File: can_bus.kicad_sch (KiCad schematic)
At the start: 1 part, among them U8 MCP2562-E-SN

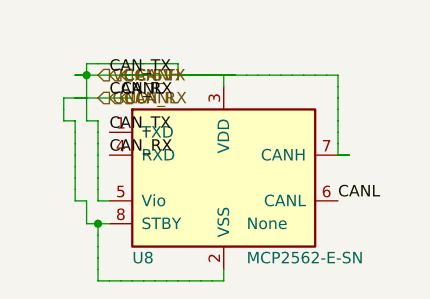
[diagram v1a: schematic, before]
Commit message: fix router map cell no more mark for pins
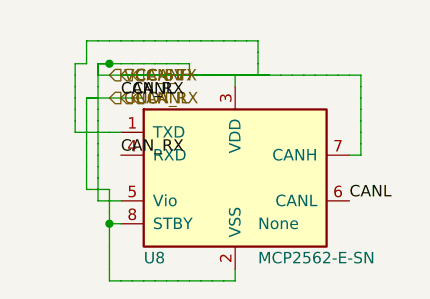
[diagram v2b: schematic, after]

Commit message: fix writer
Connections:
- net CANH: no longer U8.2 (VSS), U8.4 (RXD), U8.6 (CANL), U8.8 (STBY)
- new net CANL: U8.2 (VSS), U8.4 (RXD), U8.6 (CANL), U8.8 (STBY)

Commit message: реализована 2я занятость клетки
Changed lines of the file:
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@@
 		(instances
 			(project "Untitled"
-				(path "/1b7fa113-8fb8-4ba3-aa4e-c282a201fa61"
+				(path "/0ab84049-60df-40f5-bc1e-adacfd33f524"
 					(reference "U8")
 					(unit 1)
@@
 	(wire
 		(pts
-			(xy 21.59 29.21) (xy 21.59 25.4)
+			(xy 21.59 29.21) (xy 19.05 29.21)
 		)
 		(stroke
@@
 	(wire
 		(pts
-			(xy 21.59 25.4) (xy 19.05 25.4)
+			(xy 19.05 29.21) (xy 19.05 15.24)
 		)
 		(stroke
-			(width 0)
-			(type default)
-		)
-	)
-	(wire
-		(pts
-			(xy 19.05 25.4) (xy 19.05 15.24)
-		)
-		(stroke

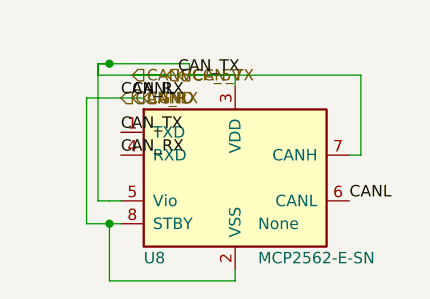
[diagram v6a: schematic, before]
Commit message: фильтр клеток для Т если там пересечение
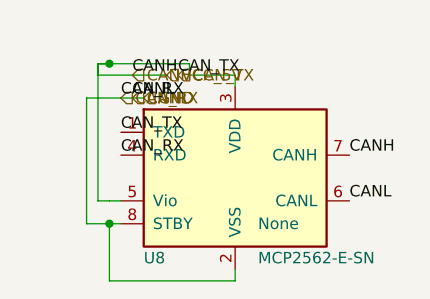
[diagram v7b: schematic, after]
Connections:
- net CANH: no longer U8.1 (TXD)
- new net CAN_TX: U8.1 (TXD)
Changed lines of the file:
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@@
 		(instances
 			(project "Untitled"
-				(path "/0ab84049-60df-40f5-bc1e-adacfd33f524"
+				(path "/e28a2808-ab3c-4497-8da1-e6c8d752bc9f"
 					(reference "U8")
 					(unit 1)
@@
 		(pts
 			(xy 21.59 35.56) (xy 21.59 29.21)
-		)
-		(stroke
-			(width 0)
-			(type default)
-		)
-	)
-	(wire
-		(pts
-			(xy 48.26 21.59) (xy 49.53 21.59)
-		)
-		(stroke
-			(width 0)
-			(type default)
-		)
-	)
-	(wire
-		(pts
-			(xy 49.53 21.59) (xy 49.53 12.7)
-		)
-		(stroke
-			(width 0)
-			(type default)
-		)
-	)
-	(wire
-		(pts
-			(xy 49.53 12.7) (xy 36.83 12.7)
-		)
-		(stroke
-			(width 0)
-			(type default)
-		)
-	)
-	(wire
-		(pts
-			(xy 36.83 12.7) (xy 24.13 12.7)
 		)
 		(stroke
@@
 		(effects
 			(font
+				(size 1.27 1.27)
+			)
+			(justify left bottom)
+		)
+	)
+	(label "CANH"
+		(at 48.26 21.59 0.0000)
+		(effects
+			(font
+				(size 1.27 1.27)
+			)
+			(justify left bottom)
+		)
+	)
+	(label "CANH"
+		(at 24.13 12.7 0.0000)
+		(effects
+			(font

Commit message: fic placer for small schemes
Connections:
- net CANH: no longer U8.3 (VDD), U8.5 (Vio)
- net CANL: no longer U8.2 (VSS), U8.4 (RXD), U8.8 (STBY)
- new net CAN_RX: U8.4 (RXD)
- new net GND: U8.2 (VSS), U8.8 (STBY)
- new net VCC_5V: U8.3 (VDD), U8.5 (Vio)
